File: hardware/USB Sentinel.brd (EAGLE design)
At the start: 32.4 x 19.1 mm, 35 parts, among them J1 USB+SHIELD-MICROB, J2 USB+SHIELD-A-S, U1 ATMEGA32U2-QFN32, U3 MAX3421EETJ+, Y1 8MHz, Y2 12MHz

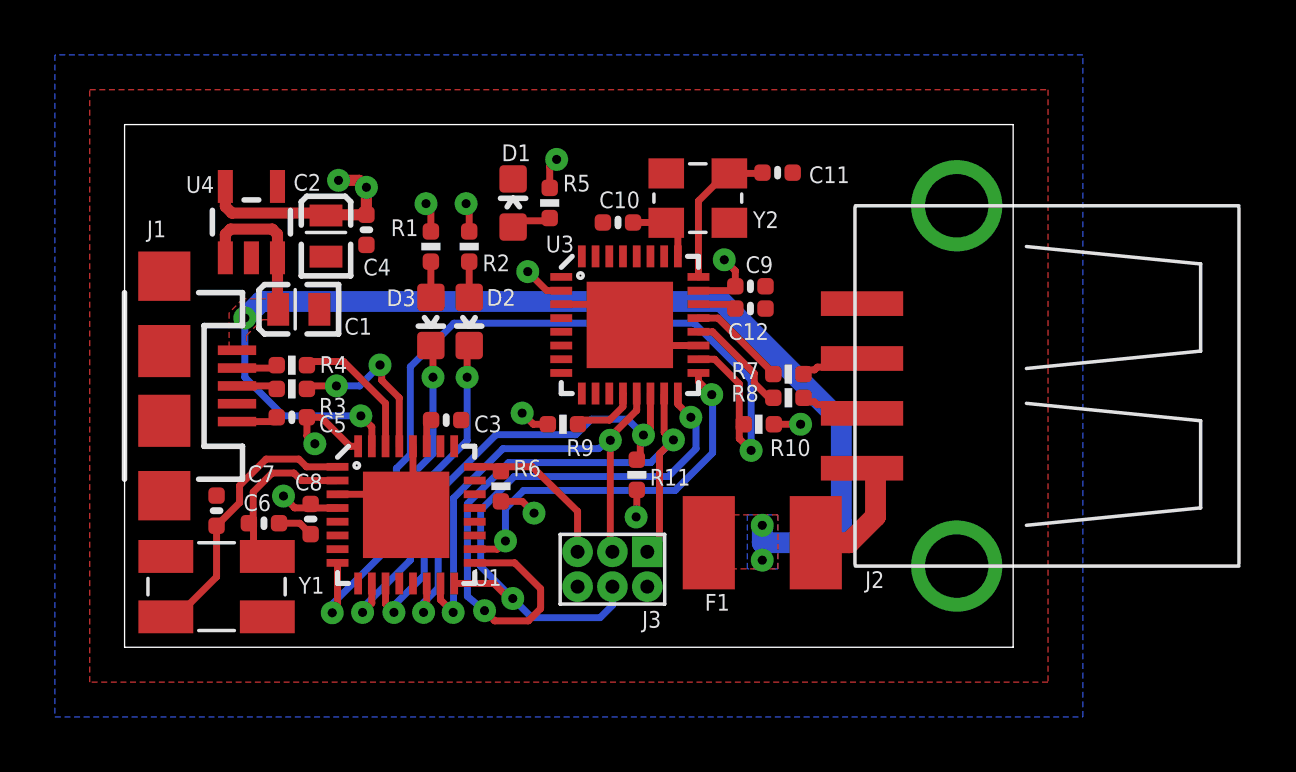
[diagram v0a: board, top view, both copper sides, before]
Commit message: Updated PCB
Changed a few things on the PCB to help with production.
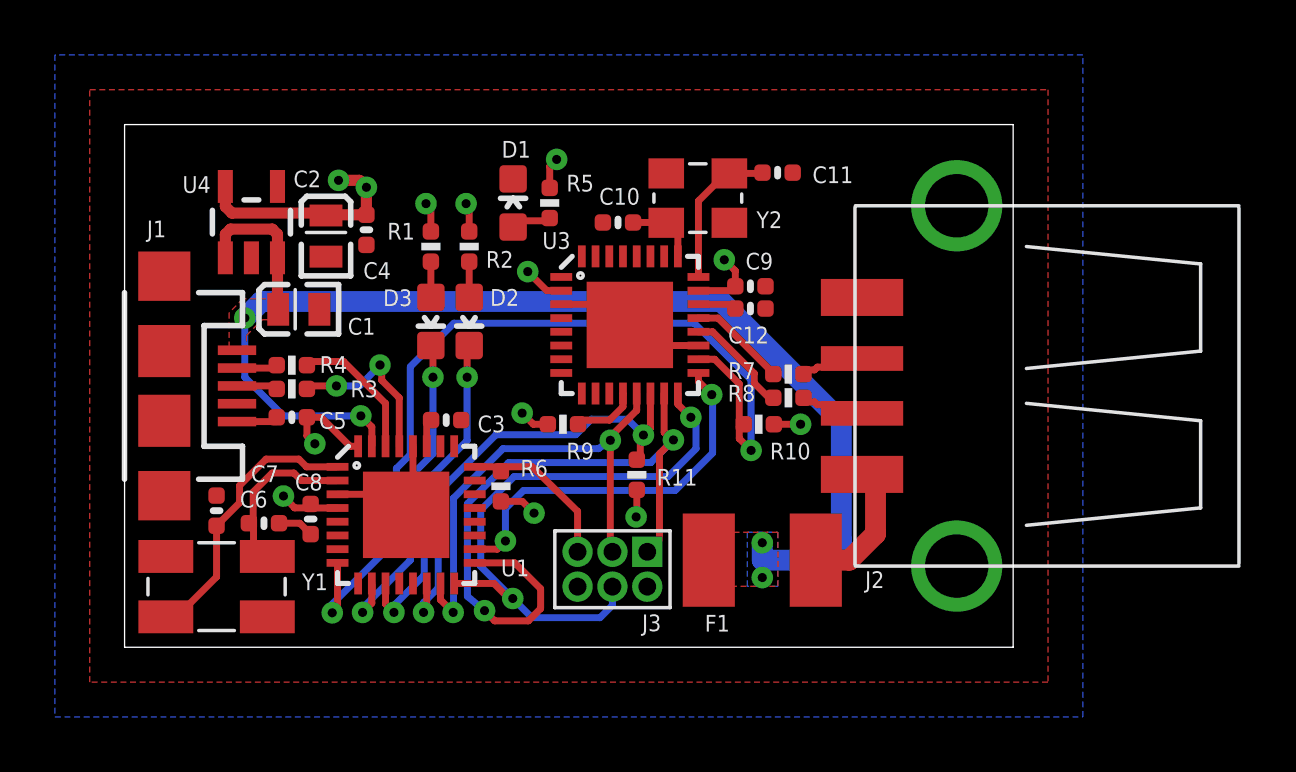
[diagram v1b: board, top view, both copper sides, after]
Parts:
- moved F1 0.64 mm to (23.2, 3.17)
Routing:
- net N$11: track 4.82 -> 5.51 mm
- net 5V: track 45.2 -> 45.9 mm
